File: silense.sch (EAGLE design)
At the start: 222 parts, among them IC1 AD8334ACPZ, IC3 LT8471EFE#PBF, J1 FMC-LPC

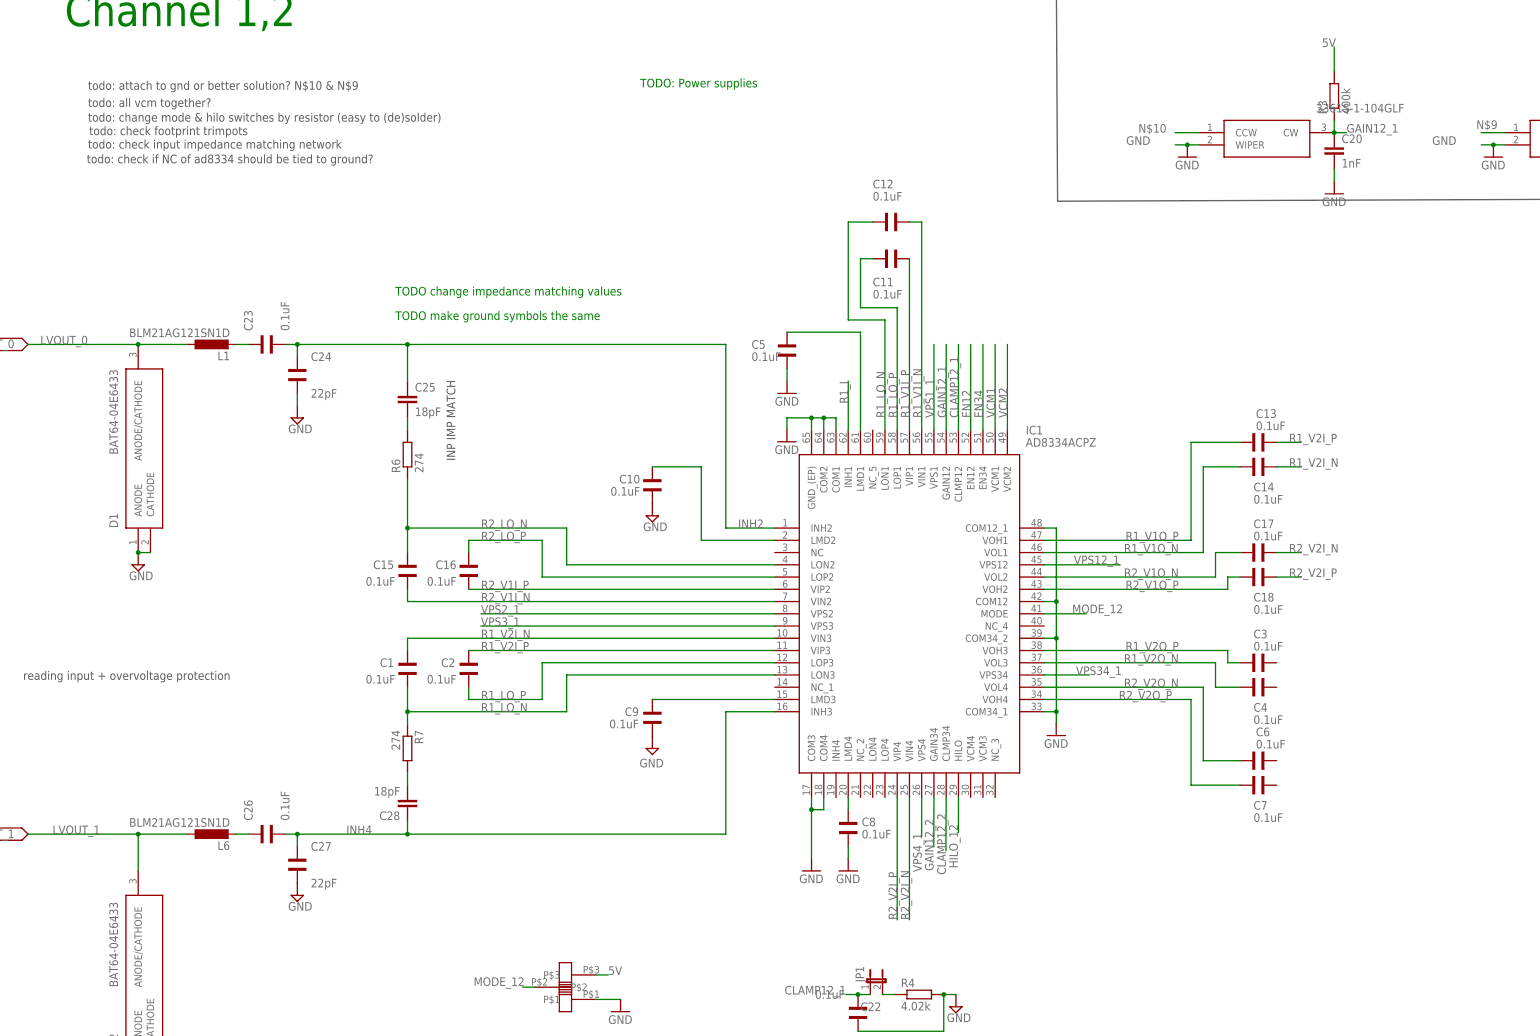
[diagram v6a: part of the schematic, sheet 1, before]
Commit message: WIP AD8334: fixed netnames, checked NC, unused channels
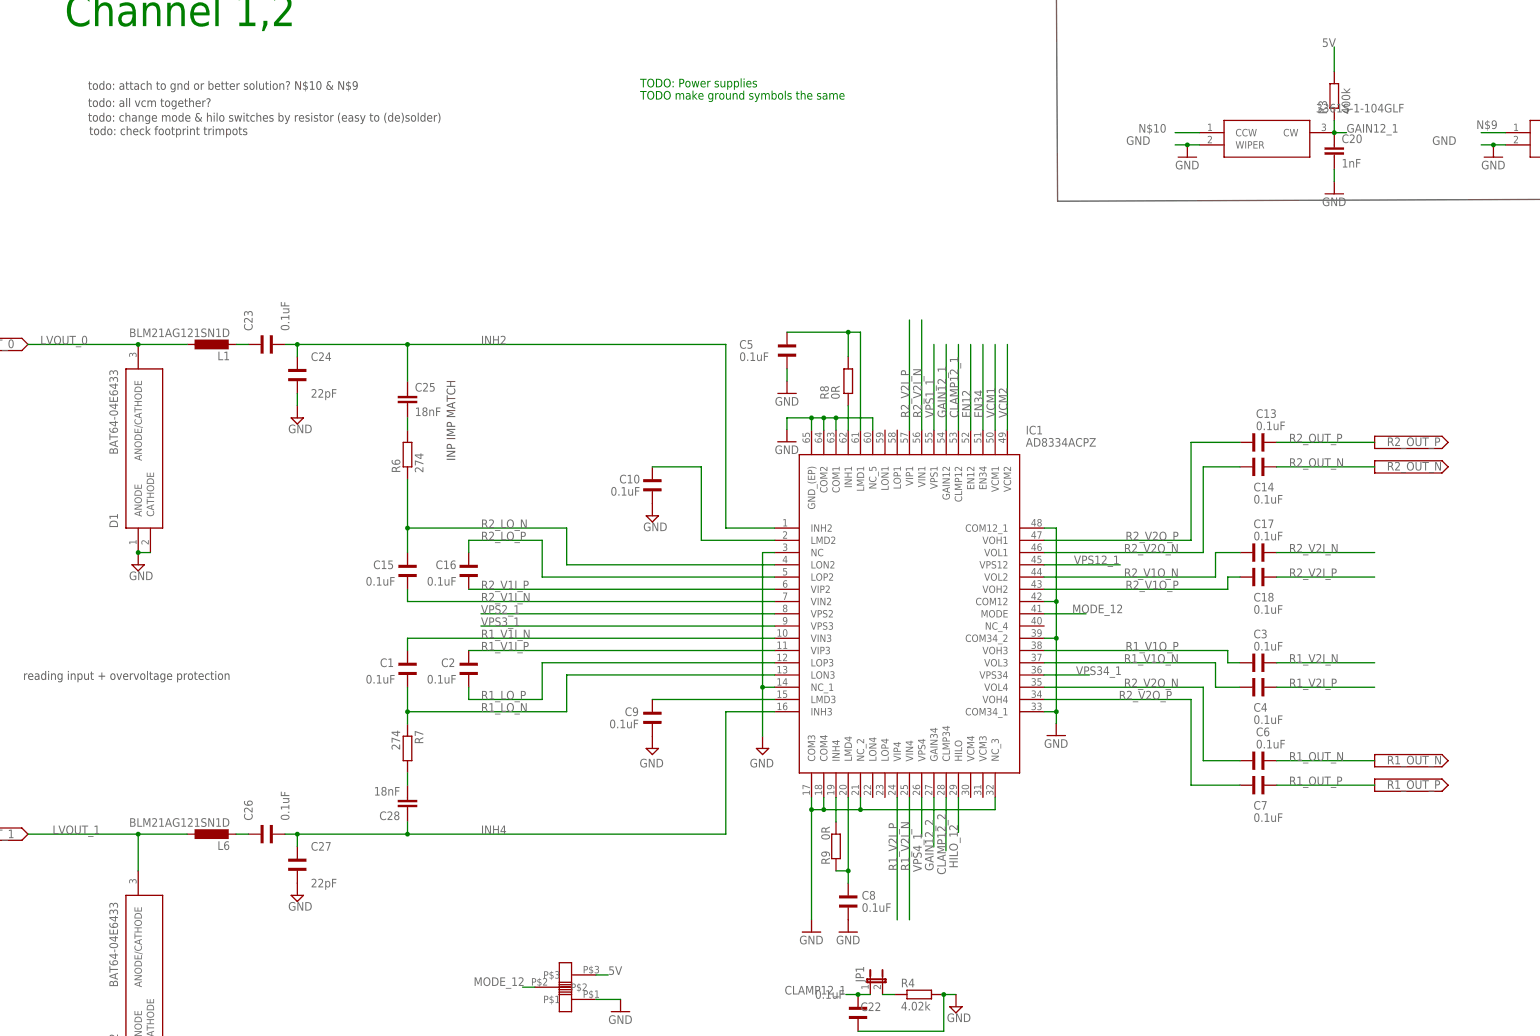
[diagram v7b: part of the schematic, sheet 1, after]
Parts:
- removed C11, C12: 0.1uF, Wurth_Elektronik_Passive_Capacitors_rev18b:WCAP-CSGP_0402_885012205037
- removed LVOUT_0, LVOUT_1, LVOUT_2, LVOUT_3, LVOUT_4, LVOUT_5, LVOUT_6, LVOUT_7: R141426, con-coax:R141426
- added R8, R9: 0R, resistor:R-EU_R0603
- C25, C28: value 18pF -> 18nF
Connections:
- new net R1_OUT_N: C6.2
- new net R1_OUT_P: C7.2
- new net R2_OUT_N: C14.2
- new net R2_OUT_P: C13.2
- net GND: now also IC1.NC, IC1.NC_1, IC1.NC_2, IC1.NC_3, IC1.NC_5; no longer LVOUT_0.2, LVOUT_1.2, LVOUT_2.2, LVOUT_3.2, LVOUT_4.2, LVOUT_5.2, LVOUT_6.2, LVOUT_7.2
- net LVOUT_0: no longer LVOUT_0.1
- net LVOUT_1: no longer LVOUT_1.1
- net LVOUT_2: no longer LVOUT_2.1
- net LVOUT_3: no longer LVOUT_3.1
- net LVOUT_4: no longer LVOUT_4.1
- net LVOUT_5: no longer LVOUT_5.1
- net LVOUT_6: no longer LVOUT_6.1
- net LVOUT_7: no longer LVOUT_7.1
- net N$1: now also R8.2
- net N$15: now also IC1.INH4, R9.2; no longer C12.1
- net N$2: now also R9.1
- net R1_I: now also R8.1
- net R1_LO_N: no longer IC1.LON1
- net R1_LO_P: no longer C11.1, IC1.LOP1
- net R1_V1I_N: now also C1.2, IC1.VIN3; no longer C12.2, IC1.VIN1
- net R1_V1I_P: now also C2.2, IC1.VIP3; no longer C11.2, IC1.VIP1
- net R1_V1O_N: now also C4.1, IC1.VOL3; no longer C14.1, IC1.VOL1
- net R1_V1O_P: now also C3.1, IC1.VOH3; no longer C13.1, IC1.VOH1
- net R1_V2I_N: now also C3.2, IC1.VIN4; no longer C1.2, C14.2, IC1.VIN3
- net R1_V2I_P: now also C4.2, IC1.VIP4; no longer C13.2, C2.2, IC1.VIP3
- net R1_V2O_N: no longer C4.1, IC1.VOL3
- net R1_V2O_P: no longer C3.1, IC1.VOH3
- net R2_V2I_N: now also IC1.VIN1; no longer IC1.VIN4
- net R2_V2I_P: now also IC1.VIP1; no longer IC1.VIP4
- net R2_V2O_N: now also C14.1, IC1.VOL1
- net R2_V2O_P: now also C13.1, IC1.VOH1
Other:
- note removed: "TODO change impedance matching values"
- note removed: "todo: check if NC of ad8334 should be tied to ground?"
- note removed: "todo: check input impedance matching network"
- moved on the sheet: C8

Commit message: basic hierachical schematic, to be refined with ports
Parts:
- removed ADC1: LTC2344-16, wouter:LTC2344-16
- removed C1, C10, C13, C14, C15, C16, C17, C18, C2, C21, C22, C23, C26, C3, C4, C5, C51, C52, C53, C54, C55, C56, C6, C7, C8, C9: 0.1uF, Wurth_Elektronik_Passive_Capacitors_rev18b:WCAP-CSGP_0402_885012205037
- removed C139, C142, C143: 0.1uf, rcl:C-EUC0402
- removed C140: 47uf, rcl:C-EUC1210
- removed C141: 2.2uf, rcl:C-EUC0402
- removed C170, C171, C172, C173, C174, C175, C176, C177, C178, C179, C180, C181, C182, C183, C184, C185, C186, C187, C188, C189, C190, C191: 220n 100V, rcl:C-EUC0805
- removed C19, C20: 1nF, rcl:C-EUC0402
- removed C24, C27: 22pF, Wurth_Elektronik_Passive_Capacitors_rev18b:WCAP-CSGP_0402_885012005009
- removed C25, C28: 18nF, rcl:C-EUC0603
- removed C30: CBEC219-3479B001C1AF, wouter:CBEC219-3479B001C1AF
- removed C39: C3216X7R1H225K160AE, samacsys:C3216X7R1H225K160AE
- removed C40, C43, C44, C47: 1206 x7r 47uF 25V, samacsys:CKG57NX5R1E476M500JH
- removed C41, C42: 0.1uF x7r 1206, samacsys:MCSH31B104K500CT
- removed C45, C46: 1206 x7r 2.2uF 25V, rcl:C-EUC1206
- removed C77, C78, C79, C80, C81, C82, C83, C84: 100n, rcl:C-EU050-025X075
- removed D0_0, D0_1, D1_0, D1_1, D2_0, D2_1, D3_0, D3_1, D4_0, D4_1, D5_0, D5_1, D6_0, D6_1, D7_0, D7_1: (no value), dfls130l-7:SBR1U200P1SBR1U200P1
- removed D1, D2: BAT64-04E6433, BAT64-04E6433:BAT64-04E6433
- removed D10, D11, D12, D5, D6, D7, D8, D9: sbr3u20sa, dfls130l-7:SBR3U20SASBR3U20SA
- removed D13, D14, D17, D18, D19, D20, D3, D4: SBR1U200P1, dfls130l-7:SBR1U200P1SBR1U200P1
- removed D15, D16, D21, D22: SBR3U20SA, dfls130l-7:SBR3U20SASBR3U20SA
- removed D25: MBRS360T3G, samacsys:MBRS360T3G
- removed D26: VS-MBRS340-M3_9AT, samacsys:VS-MBRS340-M3_9AT
- removed GAIN12_1, GAIN34_1: 3361S-1-104GLF, 3361S-1-104GLF:3361S-1-104GLF
- removed GND_1, TP2_10, TP2_11, TP2_12, TP2_5, TP2_6, TP2_7, TP2_8, TP2_9, TP2_GND1: 5019, 5019:5019
- removed HVM$1, HVM_CW$1, HVP$1, HVP_CW$1, VDDM$1, VDDP$1: R141426, con-coax:R141426
- removed IC1: AD8334ACPZ, AD8334ACPZ:AD8334ACPZ
- removed IC3: LT8471EFE#PBF, samacsys:LT8471EFE#PBF
- removed IN0_0, IN0_1, LVOUT0, T_OUT_0, T_OUT_1, T_OUT_2, T_OUT_3, T_OUT_4, T_OUT_5, T_OUT_6, T_OUT_7: 5015, keystone_5015:5015
- removed J1: FMC-LPC, wouter:FMC-LPC
- removed JP1, JP2: (no value), jumper:JP1E
- removed L1, L6: BLM21AG121SN1D, rcl:L-EUL2012C
- removed L2: 744025150, samacsys:744025150
- removed L27, L28, L29, L30, L31, L32: BLM21AG121SN1D, resistor:L-EUL2012C
- removed L7: 74437324068, samacsys:74437324068
- removed L8: 74437324100, samacsys:74437324100
- removed PGND+: GND, wirepad:3,17/1,3
- removed PGND-, PGNDD, PHVM, PHVM_CW, PHVP, PHVP_CW, PVDDM, PVDDP: (no value), wirepad:3,17/1,3
- removed POWER_BOARD_CONN: 43045-0809, con-molex-micro-fit-3_0:HEADER_POS8_43045-0809
- removed R1, R3: 400k, resistor:R-EU_R0603
- removed R17: 261k 25V, resistor:R-EU_M1206
- removed R18: 82k 25V, resistor:R-EU_M1206
- removed R19, R21: 316k, rcl:R-EU_R1206
- removed R2: 10k, rcl:R-EU_R0805
- removed R20, R22: 59k, rcl:R-EU_R1206
- removed R23, R24: 100k, rcl:R-EU_R1206
- removed R25: 187k, rcl:R-EU_R1206
- removed R4, R5: 4.02k, resistor:R-EU_R0805
- removed R43, R44, R45, R46, R47, R48, R49, R50: 1K, rcl:R-EU_0207/7
- removed R6, R7: 274, resistor:R-EU_R0603
- removed R8, R9: 0R, resistor:R-EU_R0603
- removed SLIDESWITCH1, SLIDESWITCH2: CL-SB-12A-01, wouter:CL-SB-12A-01
- removed SLIDESWITCH10, SLIDESWITCH11, SLIDESWITCH7, SLIDESWITCH9: CL-SB-22A-01, wouter:CL-SB-22A-01
- removed STHV_0: STHV800, wouter:STHV800
- removed X10, X11, X12, X2, X3, X4, X5, X9: (no value), con-phoenix-254:MPT2
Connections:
- removed net /CS: ADC1./CS
- removed net 3P3V: J1C.3P3V@3, J1D.3P3V@2
- removed net 3V3: ADC1.OVDD, C143.1
- removed net 5V: ADC1.VDD, C142.1, L27.1, L28.1, L29.1, L30.1, L31.1, L32.1, R1.2, R3.2, SLIDESWITCH1.P$3, SLIDESWITCH2.P$3
- removed net ADIN1_N: ADC1.IN0-
- removed net ADIN1_P: ADC1.IN0+
- removed net ADIN2_N: ADC1.IN1-
- removed net ADIN2_P: ADC1.IN1+
- removed net ADIN3_N: ADC1.IN2-
- removed net ADIN3_P: ADC1.IN2+
- removed net ADIN4_N: ADC1.IN3-
- removed net ADIN4_P: ADC1.IN3+
- removed net BUSY: ADC1.BUSY
- removed net C3: IC3.C3, L2.1
- removed net CLAMP12_1: C22.1, IC1.CLMP12, JP1.1
- removed net CLAMP12_2: C21.1, IC1.CLMP34, JP2.1
- removed net CLK: STHV_0.CK
- removed net CNV: ADC1.CNV
- removed net CW: STHV_0.CW
- removed net DVDD: C182.1, R2.2, STHV_0.DVDD
- removed net E1: D26.K, IC3.E1, L7.1
- removed net E2: D25.K, IC3.E2, L8.2
- removed net EN12: IC1.EN12
- removed net EN34: IC1.EN34
- removed net ENV1_N: C78.1, D6.A, R44.2, X12-2.1
- removed net ENV1_P: C77.1, D5.C, R43.2, X12-1.1
- removed net ENV2_N: C80.1, D8.A, R46.2, X11-2.1
- removed net ENV2_P: C79.1, D7.C, R45.2, X11-1.1
- removed net ENV3_N: C82.1, D10.A, R48.2, X9-2.1
- removed net ENV3_P: C81.1, D9.C, R47.2, X9-1.1
- removed net ENV4_N: C84.1, D12.A, R50.2, X10-2.1
- removed net ENV4_P: C83.1, D11.C, R49.2, X10-1.1
- removed net FB1: IC3.FB1, R19.1, R20.2
- removed net FB2: IC3.FB2, R21.1, R22.2
- removed net GAIN12_1: C20.1, GAIN12_1.CW, IC1.GAIN12, R3.1
- removed net GAIN12_2: C19.1, GAIN34_1.CW, IC1.GAIN34, R1.1
- removed net GND: ADC1.GND, ADC1.GND$2, ADC1.GND$3, ADC1.GND$4, ADC1.GND$5, ADC1.GND$6, ADC1.GND$7, ADC1.LVDS/(/CMOS), ADC1.PD, C10.1, C139.2, C140.2, C141.2, C142.2, C143.2, C170.2, C171.2, C172.2, C173.2, C174.2, C175.2, C176.2, C177.1, C178.1, C179.1, C180.2, C181.2, C182.2, C183.2, C184.2, C185.2, C186.2, C187.2, C188.2, C189.1, C19.2, C190.1, C191.1, C20.2, C21.2, C22.2, C24.1, C27.1, C30.1, C30.34, C30.35, C30.68, C39.2, C40.1, C41.1, C42.2, C43.1, C44.1, C45.2, C46.1, C47.2, C5.2, C51.1, C52.1, C53.1, C54.1, C55.1, C56.1, C77.2, C78.2, C79.2, C8.1, C80.2, C81.2, C82.2, C83.2, C84.2, C9.1, D1.ANODE, D1.CATHODE, D2.ANODE, D2.CATHODE, D26.A, GAIN12_1.WIPER, GAIN34_1.WIPER, GND_1.TP, HVM$1.2, HVM_CW$1.2, HVP$1.2, HVP_CW$1.2, IC1.COM1, IC1.COM12, IC1.COM12_1, IC1.COM2, IC1.COM3, IC1.COM34_1, IC1.COM34_2, IC1.COM4, IC1.GND_(EP), IC1.NC, IC1.NC_1, IC1.NC_2, IC1.NC_3, IC1.NC_5, IC3.EP, IC3.GND_1, IC3.GND_2, IC3.GND_3, IC3.SYNC, J1C.GND@41, J1C.GND@42, J1C.GND@43, J1C.GND@44, J1C.GND@45, J1C.GND@46, J1C.GND@47, J1C.GND@48, J1C.GND@49, J1C.GND@50, J1C.GND@51, J1C.GND@52, J1C.GND@53, J1C.GND@54, J1C.GND@55, J1C.GND@56, J1C.GND@57, J1C.GND@58, J1C.GND@59, J1C.GND@60, J1D.GND@28, J1D.GND@29, J1D.GND@30, J1D.GND@31, J1D.GND@32, J1D.GND@33, J1D.GND@34, J1D.GND@35, J1D.GND@36, J1D.GND@37, J1D.GND@38, J1D.GND@39, J1D.GND@40, J1G.GND@13, J1G.GND@14, J1G.GND@15, J1G.GND@16, J1G.GND@17, J1G.GND@18, J1G.GND@19, J1G.GND@20, J1G.GND@21, J1G.GND@22, J1G.GND@23, J1G.GND@24, J1G.GND@25, J1G.GND@26, J1G.GND@27, J1H.GND, J1H.GND@1, J1H.GND@10, J1H.GND@11, J1H.GND@12, J1H.GND@2, J1H.GND@3, J1H.GND@4, J1H.GND@5, J1H.GND@6, J1H.GND@7, J1H.GND@8, J1H.GND@9, L8.1, PGND+.P, PGND-.P, PGNDD.P, POWER_BOARD_CONN.4, POWER_BOARD_CONN.8, R18.1, R20.1, R22.1, R25.2, R4.2, R43.1, R44.1, R45.1, R46.1, R47.1, R48.1, R49.1, R5.2, R50.1, SLIDESWITCH1.P$1, SLIDESWITCH2.P$1, STHV_0.AGND, STHV_0.DGND, STHV_0.GND_PWR@1, STHV_0.GND_PWR@2, STHV_0.GND_PWR@3, STHV_0.GND_PWR@4, TP2_GND1.TP, VDDM$1.2, VDDP$1.2
- removed net HILO_12: IC1.HILO, SLIDESWITCH2.P$2
- removed net HVM: C183.1, C184.1, C185.1, C186.1, C187.1, C188.1, D0_1.A, D18.A, D1_1.A, D2_1.A, D3_1.A, D4.A, D4_1.A, D5_1.A, D6_1.A, D7_1.A, POWER_BOARD_CONN.5, STHV_0.HVM@1, STHV_0.HVM@2, STHV_0.HVM@3, STHV_0.HVM@4, STHV_0.HVM@5
- removed net HVM_CW: C189.2, C190.2, C191.2, D17.A, D3.A, POWER_BOARD_CONN.6, STHV_0.HVM_CW
- removed net HVP: C171.1, C172.1, C173.1, C174.1, C175.1, C176.1, D0_0.C, D13.C, D19.C, D1_0.C, D2_0.C, D3_0.C, D4_0.C, D5_0.C, D6_0.C, D7_0.C, POWER_BOARD_CONN.1, STHV_0.HVP@1, STHV_0.HVP@2, STHV_0.HVP@3, STHV_0.HVP@4, STHV_0.HVP@5
- removed net HVP_CW: C177.2, C178.2, C179.2, C40.2, C45.1, C46.2, D14.C, D20.C, IC3.C1, IC3.C2, L2.2, POWER_BOARD_CONN.2, R17.1, R18.2, R23.1, R24.2, STHV_0.HVP_CW
- removed net IN0_0: J1G.LA00_P_CC, STHV_0.IN1_0
- removed net IN0_1: J1G.LA00_N_CC, STHV_0.IN1_1
- removed net IN10_0: J1G.LA20_P
- removed net IN10_1: J1G.LA20_N
- removed net IN11_0: J1H.LA19_P
- removed net IN11_1: J1H.LA19_N
- removed net IN12_0: J1G.LA22_P
- removed net IN12_1: J1G.LA22_N
- removed net IN13_0: J1H.LA21_P
- removed net IN13_1: J1H.LA21_N
- removed net IN14_0: J1G.LA25_P
- removed net IN14_1: J1G.LA25_N
- removed net IN15_0: J1H.LA24_P
- removed net IN15_1: J1H.LA24_N
- removed net IN1_0: J1H.LA02_P, STHV_0.IN1_0, STHV_0.IN2_0
- removed net IN1_1: J1H.LA02_N, STHV_0.IN1_1, STHV_0.IN2_1
- removed net IN2_0: J1G.LA03_P, STHV_0.IN2_0, STHV_0.IN3_0
- removed net IN2_1: J1G.LA03_N, STHV_0.IN2_1, STHV_0.IN3_1
- removed net IN3_0: J1H.LA04_P, STHV_0.IN3_0, STHV_0.IN4_0
- removed net IN3_1: J1H.LA04_N, STHV_0.IN3_1, STHV_0.IN4_1
- removed net IN4_0: J1G.LA08_P, STHV_0.IN4_0, STHV_0.IN5_0
- removed net IN4_1: J1G.LA08_N, STHV_0.IN4_1, STHV_0.IN5_1
- removed net IN5_0: J1H.LA07_P, STHV_0.IN5_0, STHV_0.IN6_0
- removed net IN5_1: J1H.LA07_N, STHV_0.IN5_1, STHV_0.IN6_1
- removed net IN6_0: J1G.LA12_P, STHV_0.IN6_0, STHV_0.IN7_0
- removed net IN6_1: J1G.LA12_N, STHV_0.IN6_1, STHV_0.IN7_1
- removed net IN7_0: J1H.LA11_P, STHV_0.IN7_0, STHV_0.IN8_0
- removed net IN7_1: J1H.LA11_N, STHV_0.IN7_1, STHV_0.IN8_1
- removed net IN8_0: J1G.LA16_P, STHV_0.IN8_0
- removed net IN8_1: J1G.LA16_N, STHV_0.IN8_1
- removed net IN9_0: J1H.LA15_P
- removed net IN9_1: J1H.LA15_N
- removed net INH2: C23.1, C24.2, C25.1, IC1.INH2
- removed net INH4: C26.1, C27.2, C28.1, IC1.INH3
- removed net INX_1_0: IN0_1.TP
- removed net LA28_N: J1H.LA28_N
- removed net LA28_P: J1H.LA28_P
- removed net LA30_N: J1H.LA30_N
- removed net LA30_P: J1H.LA30_P
- removed net LA32_N: J1H.LA32_N
- removed net LA32_P: J1H.LA32_P
- removed net LVOUT_0: D1.ANODE/CATHODE, L1.1, LVOUT0.TP, STHV_0.LVOUT_1
- removed net LVOUT_1: D2.ANODE/CATHODE, L6.1, STHV_0.LVOUT_2
- removed net LVOUT_2: STHV_0.LVOUT_3
- removed net LVOUT_3: STHV_0.LVOUT_4
- removed net LVOUT_4: STHV_0.LVOUT_5
- removed net LVOUT_5: STHV_0.LVOUT_6
- removed net LVOUT_6: STHV_0.LVOUT_7
- removed net LVOUT_7: STHV_0.LVOUT_8
- removed net MODE_12: IC1.MODE, SLIDESWITCH1.P$2
- removed net N$1: C5.1, IC1.LMD1, R8.2
- removed net N$10: GAIN12_1.CCW
- removed net N$11: C23.2, L1.2
- removed net N$12: C25.2, R6.2
- removed net N$13: C26.2, L6.2
- removed net N$14: C28.2, R7.2
- removed net N$15: IC1.INH4, R9.2
- removed net N$17: D3.C, HVM_CW$1.1
- removed net N$18: D4.C, HVM$1.1
- removed net N$19: D13.A, HVP$1.1
- removed net N$2: C8.2, IC1.LMD4, R9.1
- removed net N$20: D14.A, HVP_CW$1.1
- removed net N$21: D15.A, VDDP$1.1
- removed net N$22: D16.C, VDDM$1.1
- removed net N$23: R2.1, STHV_0.THSD
- removed net N$24: C170.1, STHV_0.SUB
- removed net N$25: D19.A, PHVP.P
- removed net N$26: D20.A, PHVP_CW.P
- removed net N$27: D21.A, PVDDP.P
- removed net N$28: D22.C, PVDDM.P
- removed net N$3: D17.C, PHVM_CW.P
- removed net N$4: D18.C, PHVM.P
- removed net N$5: C10.2, IC1.LMD2
- removed net N$6: C9.2, IC1.LMD3
- removed net N$7: JP1.2, R4.1
- removed net N$8: JP2.2, R5.1
- removed net N$81: ADC1.REFIN, C139.1
- removed net N$82: ADC1.REFBUF, C140.1
- removed net N$83: ADC1.VDDLBYP, C141.1
- removed net N$9: GAIN34_1.CCW
- removed net N5V: C44.2, D25.A, R21.2
- removed net OUT_0: C30.2, D0_0.A, D0_1.C, STHV_0.XDCR_1, T_OUT_0.TP
- removed net OUT_1: C30.3, D1_0.A, D1_1.C, STHV_0.XDCR_2, T_OUT_1.TP
- removed net OUT_10: C30.12
- removed net OUT_11: C30.13
- removed net OUT_12: C30.14
- removed net OUT_13: C30.15
- removed net OUT_14: C30.16
- removed net OUT_15: C30.17
- removed net OUT_16: C30.18
- removed net OUT_17: C30.19
- removed net OUT_18: C30.20
- removed net OUT_19: C30.21
- removed net OUT_2: C30.4, D2_0.A, D2_1.C, STHV_0.XDCR_3, T_OUT_2.TP
- removed net OUT_20: C30.22
- removed net OUT_21: C30.23
- removed net OUT_22: C30.24
- removed net OUT_23: C30.25
- removed net OUT_24: C30.26
- removed net OUT_25: C30.27
- removed net OUT_26: C30.28
- removed net OUT_27: C30.29
- removed net OUT_28: C30.30
- removed net OUT_29: C30.31
- removed net OUT_3: C30.5, D3_0.A, D3_1.C, STHV_0.XDCR_4, T_OUT_3.TP
- removed net OUT_30: C30.32
- removed net OUT_31: C30.33
- removed net OUT_32: C30.36
- removed net OUT_33: C30.37
- removed net OUT_34: C30.38
- removed net OUT_35: C30.39
- removed net OUT_36: C30.40
- removed net OUT_37: C30.41
- removed net OUT_38: C30.42
- removed net OUT_39: C30.43
- removed net OUT_4: C30.6, D4_0.A, D4_1.C, STHV_0.XDCR_5, T_OUT_4.TP
- removed net OUT_40: C30.44
- removed net OUT_41: C30.45
- removed net OUT_42: C30.46
- removed net OUT_43: C30.47
- removed net OUT_44: C30.48
- removed net OUT_45: C30.49
- removed net OUT_46: C30.50
- removed net OUT_47: C30.51
- removed net OUT_48: C30.52
- removed net OUT_49: C30.53
- removed net OUT_5: C30.7, D5_0.A, D5_1.C, STHV_0.XDCR_6, T_OUT_5.TP
- removed net OUT_50: C30.54
- removed net OUT_51: C30.55
- removed net OUT_52: C30.56
- removed net OUT_53: C30.57
- removed net OUT_54: C30.58
- removed net OUT_55: C30.59
- removed net OUT_56: C30.60
- removed net OUT_57: C30.61
- removed net OUT_58: C30.62
- removed net OUT_59: C30.63
- removed net OUT_6: C30.8, D6_0.A, D6_1.C, STHV_0.XDCR_7, T_OUT_6.TP
- removed net OUT_60: C30.64
- removed net OUT_61: C30.65
- removed net OUT_62: C30.66
- removed net OUT_63: C30.67
- removed net OUT_7: C30.9, D7_0.A, D7_1.C, STHV_0.XDCR_8, T_OUT_7.TP
- removed net OUT_8: C30.10
- removed net OUT_9: C30.11
- removed net OV/UV: IC3.OV/UV, R17.2
- removed net P5V: C43.2, L7.2, R19.2
- removed net PG1: IC3.PG1, R24.1
- removed net PG2: IC3.PG2, R23.2
- removed net PWM_INT0: IN0_0.TP
- removed net R1_I: IC1.INH1, R8.1
- removed net R1_LO_N: C1.1, IC1.LON3, R7.1
- removed net R1_LO_P: C2.1, IC1.LOP3
- removed net R1_OUT_N: C6.2
- removed net R1_OUT_P: C7.2
- removed net R1_V1I_N: C1.2, IC1.VIN3
- removed net R1_V1I_P: C2.2, IC1.VIP3
- removed net R1_V1O_N: C4.1, IC1.VOL3, TP2_5.TP
- removed net R1_V1O_P: C3.1, IC1.VOH3, TP2_6.TP
- removed net R1_V2I_N: C3.2, IC1.VIN4
- removed net R1_V2I_P: C4.2, IC1.VIP4
- removed net R1_V2O_N: TP2_7.TP
- removed net R1_V2O_P: TP2_8.TP
- removed net R2_LO_N: C15.2, IC1.LON2, R6.1
- removed net R2_LO_P: C16.2, IC1.LOP2
- removed net R2_OUT_N: C14.2
- removed net R2_OUT_P: C13.2
- removed net R2_V1I_N: C15.1, IC1.VIN2
- removed net R2_V1I_P: C16.1, IC1.VIP2
- removed net R2_V1O_N: C17.1, IC1.VOL2, TP2_9.TP
- removed net R2_V1O_P: C18.1, IC1.VOH2, TP2_10.TP
- removed net R2_V2I_N: C17.2, IC1.VIN1
- removed net R2_V2I_P: C18.2, IC1.VIP1
- removed net R2_V2O_N: C14.1, C6.1, IC1.VOL1, IC1.VOL4, TP2_11.TP
- removed net R2_V2O_P: C13.1, C7.1, IC1.VOH1, IC1.VOH4, TP2_12.TP
- removed net RT: IC3.RT, R25.1
- removed net SCKI: ADC1.SCKI
- removed net SDI: ADC1.SDO-/SDI
- removed net SDO0: ADC1.SDO0
- removed net SDO1: ADC1.SDO1
- removed net SDO2: ADC1.SDO2
- removed net SDO3: ADC1.SDO3
- removed net SS1: C41.2, IC3.SS1
- removed net SS2: C42.1, IC3.SS2
- removed net VCM1: IC1.VCM1
- removed net VCM2: IC1.VCM2
- removed net VDDM: C181.1, D16.A, D22.A, POWER_BOARD_CONN.7, STHV_0.VDDM
- removed net VDDP: C180.1, D15.C, D21.C, POWER_BOARD_CONN.3, STHV_0.VDDP
- removed net VINT: C39.1, C47.1, IC3.SHOUT, IC3.VIN1, IC3.VIN2
- removed net VO1_3: SLIDESWITCH7.P$3, SLIDESWITCH7.P$6
- removed net VO1_3_N: D6.C, SLIDESWITCH7.P$5, X2-2.1
- removed net VO1_3_P: D5.A, SLIDESWITCH7.P$2, X2-1.1
- removed net VO2_3: SLIDESWITCH9.P$3, SLIDESWITCH9.P$6
- removed net VO2_3_N: D8.C, SLIDESWITCH9.P$5, X3-2.1
- removed net VO2_3_P: D7.A, SLIDESWITCH9.P$2, X3-1.1
- removed net VO3_3: SLIDESWITCH11.P$3, SLIDESWITCH11.P$6
- removed net VO3_3_N: D10.C, SLIDESWITCH11.P$5, X4-2.1
- removed net VO3_3_P: D9.A, SLIDESWITCH11.P$2, X4-1.1
- removed net VO4_3: SLIDESWITCH10.P$3, SLIDESWITCH10.P$6
- removed net VO4_3_N: D12.C, SLIDESWITCH10.P$5, X5-2.1
- removed net VO4_3_P: D11.A, SLIDESWITCH10.P$2, X5-1.1
- removed net VPS12_1: C56.2, IC1.VPS12, L32.2
- removed net VPS1_1: C55.2, IC1.VPS1, L31.2
- removed net VPS2_1: C51.2, IC1.VPS2, L27.2
- removed net VPS34_1: C54.2, IC1.VPS34, L30.2
- removed net VPS3_1: C52.2, IC1.VPS3, L28.2
- removed net VPS4_1: C53.2, IC1.VPS4, L29.2
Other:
- note added: "Silense - Main Schematic"
- note removed: "TODO: still wanted?"
